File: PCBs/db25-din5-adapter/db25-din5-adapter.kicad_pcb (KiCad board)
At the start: 2 copper layers, 53.3 x 27.3 mm, 4 parts, among them J1 DB25_Plug_MountingHoles, J2 TX/RX Straight/cross, J3 DTR/RTS Straight/cross

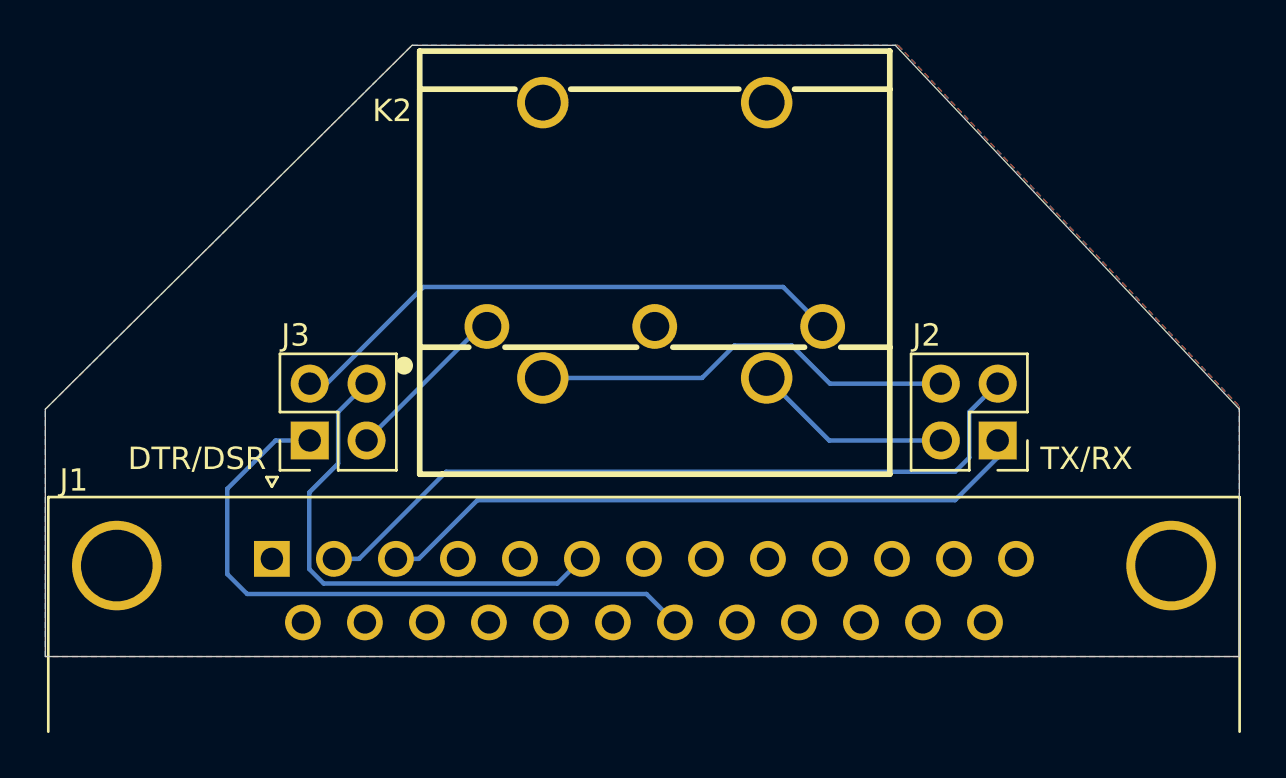
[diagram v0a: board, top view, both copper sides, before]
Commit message: Fixes (mounting holes!) and more adapters
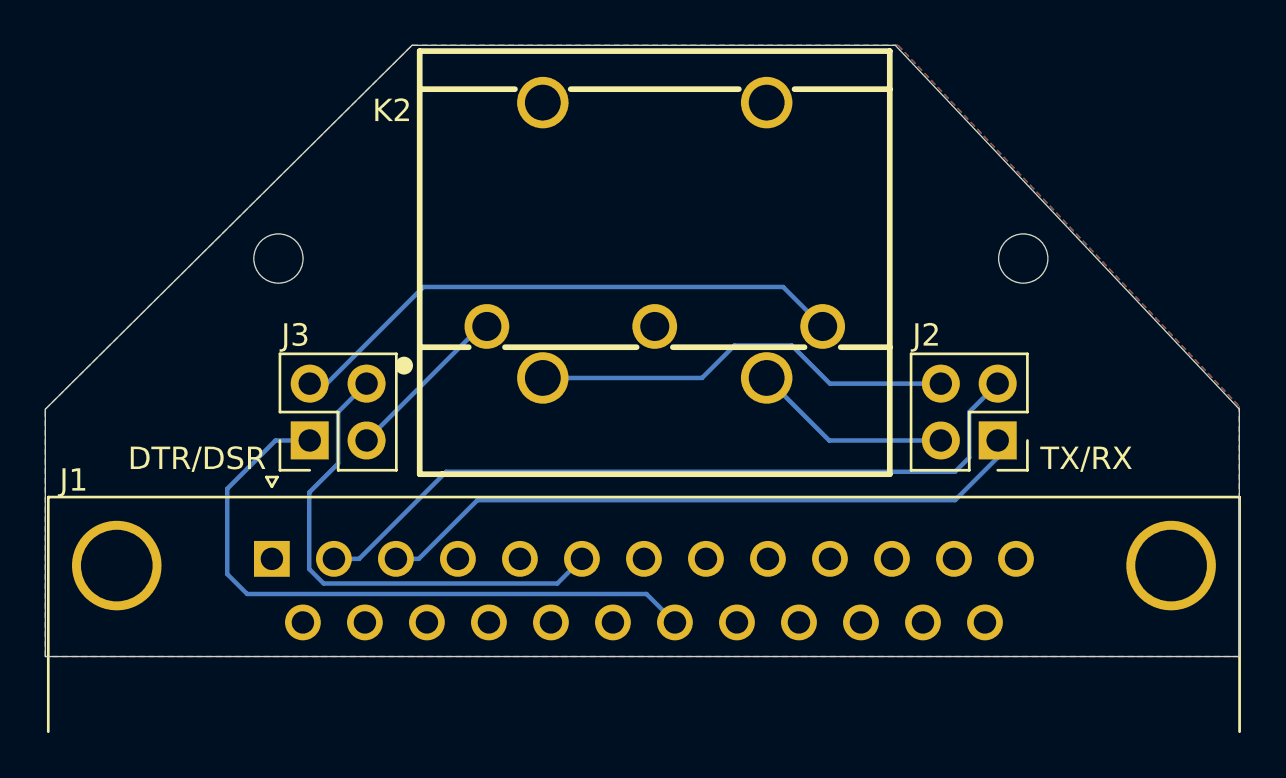
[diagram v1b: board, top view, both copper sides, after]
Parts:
- added REF**: MountingHole_2.2mm_M2, MountingHole:MountingHole_2.2mm_M2, F.Cu at (128.7, 71.2)
- added REF**: MountingHole_2.2mm_M2, MountingHole:MountingHole_2.2mm_M2, F.Cu at (95.4, 71.2)
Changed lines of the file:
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@@
 		)
+	)
+	(footprint "MountingHole:MountingHole_2.2mm_M2"
+		(layer "F.Cu")
+		(at 128.651 71.247)
+		(descr "Mounting Hole 2.2mm, M2, no annular, generated by kicad-footprint-generator mountinghole.py")
+		(tags "mountinghole M2")
+		(property "Reference" "REF**"
+			(at 0 -3.15 0)
+			(layer "F.Fab")
+			(effects
+				(font
+					(size 1 1)
+					(thickness 0.15)
+				)
+			)
+		)
+		(property "Value" "MountingHole_2.2mm_M2"
+			(at 0 3.15 0)
+			(layer "F.Fab")
+			(effects
+				(font
+					(size 1 1)
+					(thickness 0.15)
+				)
+			)
+		)
+		(property "Datasheet" ""
+			(at 0 0 0)
+			(layer "F.Fab")
+			(hide yes)
+			(effects
+				(font
+					(size 1.27 1.27)
+					(thickness 0.15)
+				)
+			)
+		)
+		(property "Description" ""
+			(at 0 0 0)
+			(layer "F.Fab")
+			(hide yes)
+			(effects
+				(font
+					(size 1.27 1.27)
+					(thickness 0.15)
+				)
+			)
+		)
+		(attr board_only exclude_from_pos_files exclude_from_bom)
+		(fp_circle
+			(center 0 0)
+			(end 2.2 0)
+			(stroke
+				(width 0.15)
+				(type solid)
+			)
+			(fill no)
+			(layer "Cmts.User")
+		)
+		(fp_circle
+			(center 0 0)
+			(end 2.45 0)
+			(stroke
+				(width 0.05)
+				(type solid)
+			)
+			(fill no)
+			(layer "F.CrtYd")
+		)
+		(fp_text user "${REFERENCE}"
+			(at 0 0 0)
+			(layer "F.Fab")
+			(effects
+				(font
+					(size 1 1)
+					(thickness 0.15)
+				)
+			)
+		)
+		(pad "" np_thru_hole circle
+			(at 0 0)
+			(size 2.2 2.2)
+			(drill 2.2)
+			(layers "*.Cu" "*.Mask")
+		)
+		(embedded_fonts no)
 	)
 	(footprint "DIN5:CONN-TH_DIN-504-M10"
@@
 		)
 	)
+	(footprint "MountingHole:MountingHole_2.2mm_M2"
+		(layer "F.Cu")
+		(at 95.377 71.247)
+		(descr "Mounting Hole 2.2mm, M2, no annular, generated by kicad-footprint-generator mountinghole.py")
+		(tags "mountinghole M2")
+		(property "Reference" "REF**"
+			(at 0 -3.15 0)
+			(layer "F.Fab")
+			(effects
+				(font
+					(size 1 1)
+					(thickness 0.15)
+				)
+			)
+		)
+		(property "Value" "MountingHole_2.2mm_M2"
+			(at 0 3.15 0)
+			(layer "F.Fab")
+			(effects
+				(font
+					(size 1 1)
+					(thickness 0.15)
+				)
+			)
+		)
+		(property "Datasheet" ""
+			(at 0 0 0)
+			(layer "F.Fab")
+			(hide yes)
+			(effects
+				(font
+					(size 1.27 1.27)
+					(thickness 0.15)
+				)
+			)
+		)
+		(property "Description" ""
+			(at 0 0 0)
+			(layer "F.Fab")
+			(hide yes)
+			(effects
+				(font
+					(size 1.27 1.27)
+					(thickness 0.15)
+				)
+			)
+		)
+		(attr board_only exclude_from_pos_files exclude_from_bom)
+		(fp_circle
+			(center 0 0)
+			(end 2.2 0)
+			(stroke
+				(width 0.15)
+				(type solid)
+			)
+			(fill no)
+			(layer "Cmts.User")
+		)
+		(fp_circle
+			(center 0 0)
+			(end 2.45 0)
+			(stroke
+				(width 0.05)
+				(type solid)
+			)
+			(fill no)
+			(layer "F.CrtYd")
+		)
+		(fp_text user "${REFERENCE}"
+			(at 0 0 0)
+			(layer "F.Fab")
+			(effects
+				(font
+					(size 1 1)
+					(thickness 0.15)
+				)
+			)
+		)
+		(pad "" np_thru_hole circle
+			(at 0 0)
+			(size 2.2 2.2)
+			(drill 2.2)
+			(layers "*.Cu" "*.Mask")
+		)
+		(embedded_fonts no)
+	)
+	(gr_line
+		(start 84.963 77.978)
+		(end 101.346 61.722)
+		(stroke
+			(width 0.05)
+			(type default)
+		)
+		(layer "Edge.Cuts")
+	)
+	(gr_line
+		(start 84.963 89.027)
+		(end 84.963 77.978)
+		(stroke
+			(width 0.05)
+			(type default)
+		)
+		(layer "Edge.Cuts")
+	)
+	(gr_line
+		(start 84.963 89.027)
+		(end 138.303 89.027)
+		(stroke
+			(width 0.05)
+			(type default)
+		)
+		(layer "Edge.Cuts")
+	)
+	(gr_line
+		(start 122.936 61.722)
+		(end 101.346 61.722)
+		(stroke
+			(width 0.05)
+			(type default)
+		)
+		(layer "Edge.Cuts")
+	)
+	(gr_line
+		(start 138.303 77.978)
+		(end 122.936 61.722)
+		(stroke
+			(width 0.05)
+			(type default)
+		)
+		(layer "Edge.Cuts")
+	)
 	(gr_line
 		(start 138.303 89.027)
@@
 		(layer "Edge.Cuts")
 	)
-	(gr_line
-		(start 84.963 89.027)
-		(end 138.303 89.027)
-		(stroke
-			(width 0.05)
-			(type default)
-		)
-		(layer "Edge.Cuts")
-	)
-	(gr_line
-		(start 138.303 77.978)
-		(end 122.936 61.722)
-		(stroke
-			(width 0.05)
-			(type default)
-		)
-		(layer "Edge.Cuts")
-	)
-	(gr_line
-		(start 122.936 61.722)
-		(end 101.346 61.722)
-		(stroke
-			(width 0.05)
-			(type default)
-		)
-		(layer "Edge.Cuts")
-	)
-	(gr_line
-		(start 84.963 89.027)
-		(end 84.963 77.978)
-		(stroke
-			(width 0.05)
-			(type default)
-		)
-		(layer "Edge.Cuts")
-	)
-	(gr_line
-		(start 84.963 77.978)
-		(end 101.346 61.722)
-		(stroke
-			(width 0.05)
-			(type default)
-		)
-		(layer "Edge.Cuts")
+	(gr_text "DTR/DSR"
+		(at 88.646 80.772 0)
+		(layer "F.SilkS")
+		(effects
+			(font
+				(size 1 1)
+				(thickness 0.1)
+			)
+			(justify left bottom)
+		)
 	)
 	(gr_text "TX/RX"
@@
 		)
 	)
-	(gr_text "DTR/DSR"
-		(at 88.646 80.772 0)
-		(layer "F.SilkS")
+	(gr_text "Apple II serial\nDB25-DIN5 adapter"
+		(at 118.999 68.58 0)
+		(layer "B.SilkS")
 		(effects
 			(font
@@
 				(thickness 0.1)
 			)
-			(justify left bottom)
+			(justify left bottom mirror)
+		)
+	)
+	(gr_text "DB25M"
+		(at 133.477 88.138 0)
+		(layer "B.SilkS")
+		(effects
+			(font
+				(size 1 1)
+				(thickness 0.1)
+			)
+			(justify left bottom mirror)
+		)
+	)
+	(gr_text "↔ Straight\n↕ Cross-over"
+		(at 118.872 71.755 0)
+		(layer "B.SilkS")
+		(effects
+			(font
+				(size 1 1)
+				(thickness 0.125)
+			)
+			(justify left bottom mirror)
+		)
+	)
+	(gr_text "DTR"
+		(at 94.615 82.804 0)
+		(layer "B.SilkS")
+		(effects
+			(font
+				(size 1 1)
+				(thickness 0.2)
+				(bold yes)
+			)
+			(justify left bottom mirror)
 		)
 	)
@@
 		)
 	)
-	(gr_text "↔ Straight\n↕ Cross-over"
-		(at 118.872 71.755 0)
-		(layer "B.SilkS")
-		(effects
-			(font
-				(size 1 1)
-				(thickness 0.125)
-			)
-			(justify left bottom mirror)
-		)
-	)
-	(gr_text "DTR"
-		(at 94.615 82.804 0)
-		(layer "B.SilkS")
-		(effects
-			(font
-				(size 1 1)
-				(thickness 0.2)
-				(bold yes)
-			)
-			(justify left bottom mirror)
-		)
-	)
 	(gr_text "TX"
 		(at 102.108 82.804 0)
@@
 			)
 			(justify left bottom mirror)
-		)
-	)
-	(gr_text "DB25M"
-		(at 133.477 88.138 0)
-		(layer "B.SilkS")
-		(effects
-			(font
-				(size 1 1)
-				(thickness 0.1)
-			)
-			(justify left bottom mirror)
-		)
-	)
-	(gr_text "Apple II serial\nDB25-DIN5 adapter"
-		(at 118.999 68.58 0)
-		(layer "B.SilkS")
-		(effects
-			(font
-				(size 1 1)
-				(thickness 0.1)
-			)
-			(justify left bottom mirror)

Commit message: Update Quicktake doc and PCBs
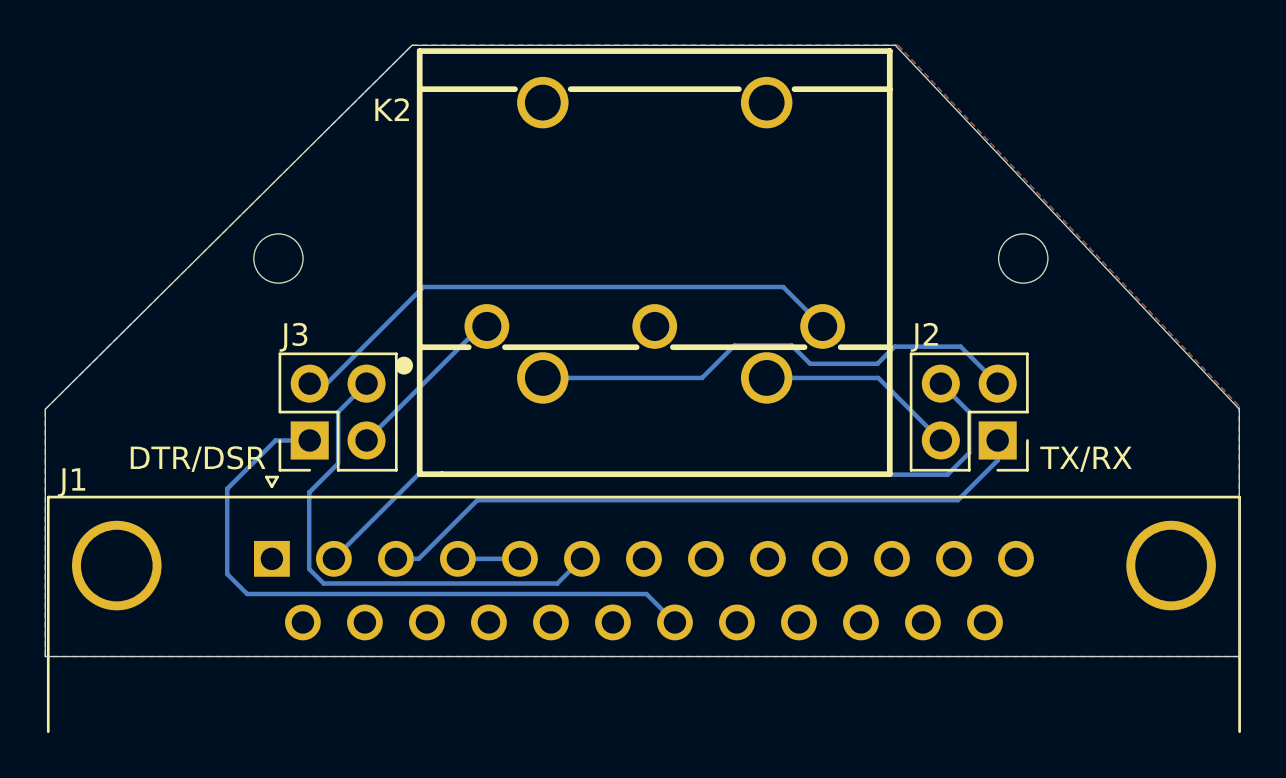
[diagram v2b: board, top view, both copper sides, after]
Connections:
- J1 pad 4: RTS -> CTS
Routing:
- net TX: track 53.6 -> 56.7 mm
- net CTS: track 0.00 -> 2.77 mm
- net RX: track 38.5 -> 39.3 mm
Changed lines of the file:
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@@
 	(net 21 "unconnected-(J1-P18-Pad18)")
 	(net 22 "unconnected-(J1-Pad9)")
-	(net 23 "RTS")
-	(net 24 "unconnected-(J1-P14-Pad14)")
-	(net 25 "DTR")
+	(net 23 "unconnected-(J1-P14-Pad14)")
+	(net 24 "DTR")
 	(footprint "Connector_Dsub:DSUB-25_Male_Horizontal_P2.77x2.84mm_EdgePinOffset4.94mm_Housed_MountingHolesOffset7.48mm"
 		(layer "F.Cu")
@@
 			(layers "*.Cu" "*.Mask")
 			(remove_unused_layers no)
-			(net 23 "RTS")
+			(net 6 "CTS")
 			(pinfunction "4")
 			(pintype "passive")
@@
 			(layers "*.Cu" "*.Mask")
 			(remove_unused_layers no)
-			(net 24 "unconnected-(J1-P14-Pad14)")
+			(net 23 "unconnected-(J1-P14-Pad14)")
 			(pinfunction "P14")
 			(pintype "passive")
@@
 			(layers "*.Cu" "*.Mask")
 			(remove_unused_layers no)
-			(net 25 "DTR")
+			(net 24 "DTR")
 			(pinfunction "P20")
 			(pintype "passive")
@@
 			(layers "*.Cu" "*.Mask")
 			(remove_unused_layers no)
-			(net 25 "DTR")
+			(net 24 "DTR")
 			(pinfunction "1")
 			(pintype "unspecified")
@@
 			(layers "*.Cu" "*.Mask")
 			(remove_unused_layers no)
-			(net 25 "DTR")
+			(net 24 "DTR")
 			(pinfunction "Pin_1")
 			(pintype "passive")
@@
 			(layers "*.Cu" "*.Mask")
 			(remove_unused_layers no)
-			(net 25 "DTR")
+			(net 24 "DTR")
 			(pinfunction "Pin_3")
 			(pintype "passive")
@@
 	(segment
 		(start 104.267 82.042)
-		(end 125.603 82.042)
+		(end 125.73 82.042)
+		(width 0.2)
+		(layer "B.Cu")
+		(net 3)
+	)
+	(segment
+		(start 122.174 76.581)
+		(end 124.968 79.375)
+		(width 0.2)
+		(layer "B.Cu")
+		(net 3)
+	)
+	(segment
+		(start 125.73 82.042)
+		(end 127.508 80.264)
+		(width 0.2)
+		(layer "B.Cu")
+		(net 3)
+	)
+	(segment
+		(start 101.646 84.663)
+		(end 104.267 82.042)
+		(width 0.2)
+		(layer "B.Cu")
+		(net 3)
+	)
+	(segment
+		(start 127.508 80.264)
+		(end 127.508 79.375)
+		(width 0.2)
+		(layer "B.Cu")
+		(net 3)
+	)
+	(segment
+		(start 117.188 76.581)
+		(end 122.174 76.581)
+		(width 0.2)
+		(layer "B.Cu")
+		(net 3)
+	)
+	(segment
+		(start 127.508 80.137)
+		(end 127.508 79.375)
 		(width 0.2)
 		(layer "B.Cu")
@@
 	)
 	(segment
-		(start 101.646 84.663)
-		(end 104.267 82.042)
-		(width 0.2)
-		(layer "B.Cu")
-		(net 3)
-	)
-	(segment
-		(start 125.603 82.042)
-		(end 127.508 80.137)
-		(width 0.2)
-		(layer "B.Cu")
-		(net 3)
-	)
-	(segment
-		(start 117.188 76.581)
-		(end 119.982 79.375)
-		(width 0.2)
-		(layer "B.Cu")
-		(net 3)
-	)
-	(segment
-		(start 127.508 80.137)
-		(end 127.508 79.375)
-		(width 0.2)
-		(layer "B.Cu")
-		(net 3)
-	)
-	(segment
-		(start 119.982 79.375)
-		(end 124.968 79.375)
-		(width 0.2)
-		(layer "B.Cu")
-		(net 3)
-	)
-	(segment
-		(start 102.87 80.772)
-		(end 125.603 80.772)
+		(start 107.188 76.581)
+		(end 114.3 76.581)
 		(width 0.2)
 		(layer "B.Cu")
@@
 	)
 	(segment
-		(start 126.238 78.105)
-		(end 127.508 76.835)
+		(start 115.751 75.13)
+		(end 118.31 75.13)
 		(width 0.2)
 		(layer "B.Cu")
@@
 	)
 	(segment
-		(start 98.979 84.663)
-		(end 102.87 80.772)
-		(width 0.2)
-		(layer "B.Cu")
-		(net 4)
-	)
-	(segment
-		(start 120.015 76.835)
-		(end 124.968 76.835)
-		(width 0.2)
-		(layer "B.Cu")
-		(net 4)
-	)
-	(segment
-		(start 97.855 84.663)
-		(end 98.979 84.663)
-		(width 0.2)
-		(layer "B.Cu")
-		(net 4)
-	)
-	(segment
 		(start 127.762 76.835)
 		(end 127.508 76.835)
@@
 	)
 	(segment
-		(start 125.603 80.772)
-		(end 126.238 80.137)
+		(start 126.238 79.934173)
+		(end 126.238 78.105)
+		(width 0.2)
+		(layer "B.Cu")
+		(net 4)
+	)
+	(segment
+		(start 125.273173 80.899)
+		(end 126.238 79.934173)
+		(width 0.2)
+		(layer "B.Cu")
+		(net 4)
+	)
+	(segment
+		(start 101.619 80.899)
+		(end 125.273173 80.899)
+		(width 0.2)
+		(layer "B.Cu")
+		(net 4)
+	)
+	(segment
+		(start 119.126 75.946)
+		(end 122.14225 75.946)
 		(width 0.2)
 		(layer "B.Cu")
@@
 	)
 	(segment
-		(start 107.188 76.581)
-		(end 114.3 76.581)
+		(start 125.857 75.184)
+		(end 127.508 76.835)
 		(width 0.2)
 		(layer "B.Cu")
@@
 	)
 	(segment
-		(start 126.238 80.137)
-		(end 126.238 78.105)
+		(start 97.855 84.663)
+		(end 101.619 80.899)
 		(width 0.2)
 		(layer "B.Cu")
@@
 	)
 	(segment
+		(start 122.90425 75.184)
+		(end 125.857 75.184)
+		(width 0.2)
+		(layer "B.Cu")
+		(net 4)
+	)
+	(segment
 		(start 118.31 75.13)
-		(end 120.015 76.835)
+		(end 119.126 75.946)
 		(width 0.2)
 		(layer "B.Cu")
@@
 	)
 	(segment
-		(start 115.751 75.13)
-		(end 118.31 75.13)
+		(start 126.238 78.105)
+		(end 124.968 76.835)
 		(width 0.2)
 		(layer "B.Cu")
 		(net 4)
+	)
+	(segment
+		(start 122.14225 75.946)
+		(end 122.90425 75.184)
+		(width 0.2)
+		(layer "B.Cu")
+		(net 4)
+	)
+	(segment
+		(start 103.395 84.663)
+		(end 106.165 84.663)
+		(width 0.2)
+		(layer "B.Cu")
+		(net 6)
 	)
 	(segment
@@
 		(width 0.2)
 		(layer "B.Cu")
-		(net 25)
+		(net 24)
 	)
 	(segment
@@
 		(width 0.2)
 		(layer "B.Cu")
-		(net 25)
+		(net 24)
 	)
 	(segment
@@
 		(width 0.2)
 		(layer "B.Cu")
-		(net 25)
+		(net 24)
 	)
 	(segment
@@
 		(width 0.2)
 		(layer "B.Cu")
-		(net 25)
+		(net 24)
 	)
 	(segment
@@
 		(width 0.2)
 		(layer "B.Cu")
-		(net 25)
+		(net 24)
 	)
 	(segment
@@
 		(width 0.2)
 		(layer "B.Cu")
-		(net 25)
+		(net 24)
 	)
 	(segment
@@
 		(width 0.2)
 		(layer "B.Cu")
-		(net 25)
+		(net 24)
 	)
 	(segment
@@
 		(width 0.2)
 		(layer "B.Cu")
-		(net 25)
+		(net 24)
 	)
 	(zone
